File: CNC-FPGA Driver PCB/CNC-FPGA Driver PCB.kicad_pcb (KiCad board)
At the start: 2 copper layers, 73.5 x 87 mm, 16 parts

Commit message: updated pcb traces
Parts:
- -  12V  +: renamed from 12V Power Supply
- A4988 X Axis Driver: value A4988 Stepper Driver -> A4988 N Axis Driver
- C1: renamed from 100[µF]; value C1 -> +100[µF]-
- renumbered 100[µF] to +100[µF]-
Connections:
- A4988 X Axis Driver pad 10: /SLP -> +3.3V
- A4988 Y Axis Driver pad 10: /SLP -> +3.3V
- A4988 Z Axis Driver pad 10: /SLP -> +3.3V
- JA pad 1: /MS1 -> /MS1 
- JA pad 10: +3.3V -> /LS+
- LimitSwitchX pad 1: +3.3V -> /LS+
- LimitSwitchY pad 1: +3.3V -> /LS+
- LimitSwitchZ pad 1: +3.3V -> /LS+
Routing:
- net /LS+: track 0.00 -> 4.84 mm
- net +3.3V: track 14.5 -> 9.68 mm
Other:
- board size 73.5 x 87 mm -> 70 x 85 mm

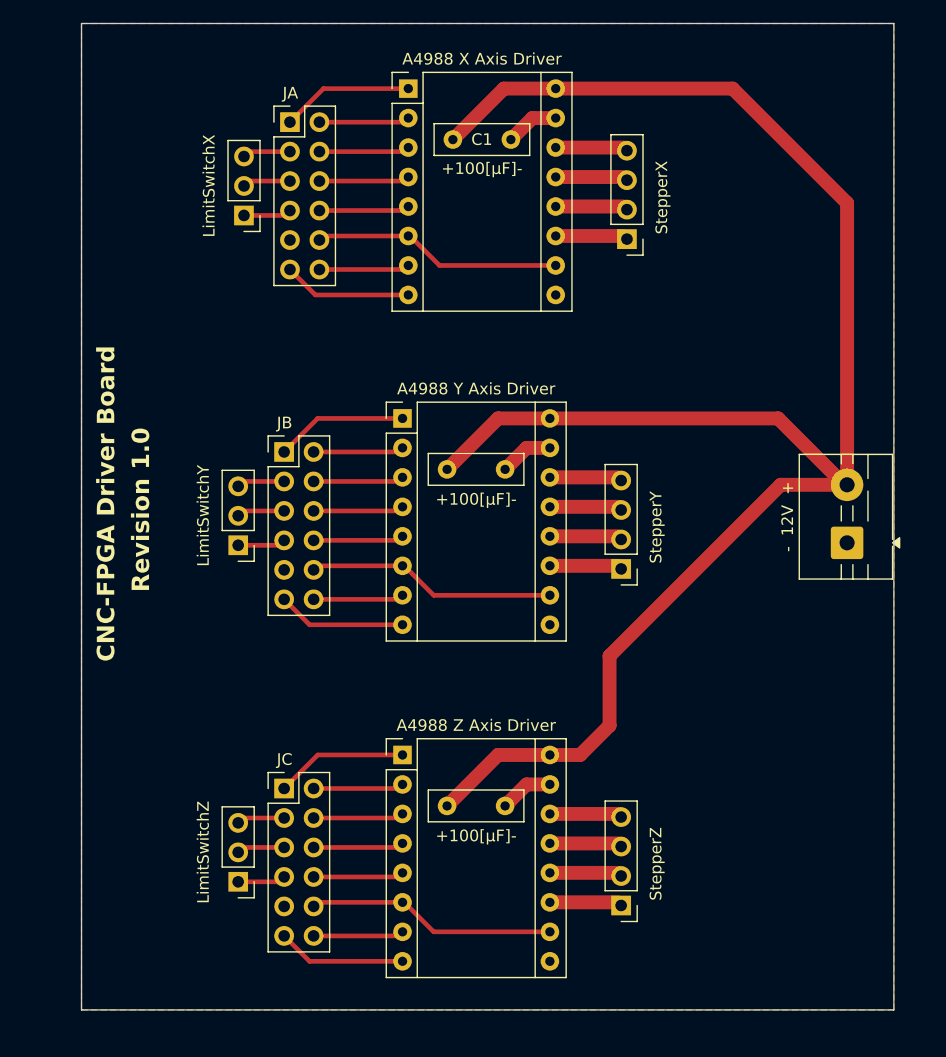
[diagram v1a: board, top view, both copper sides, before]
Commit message: added M2 mounting holes to pcb
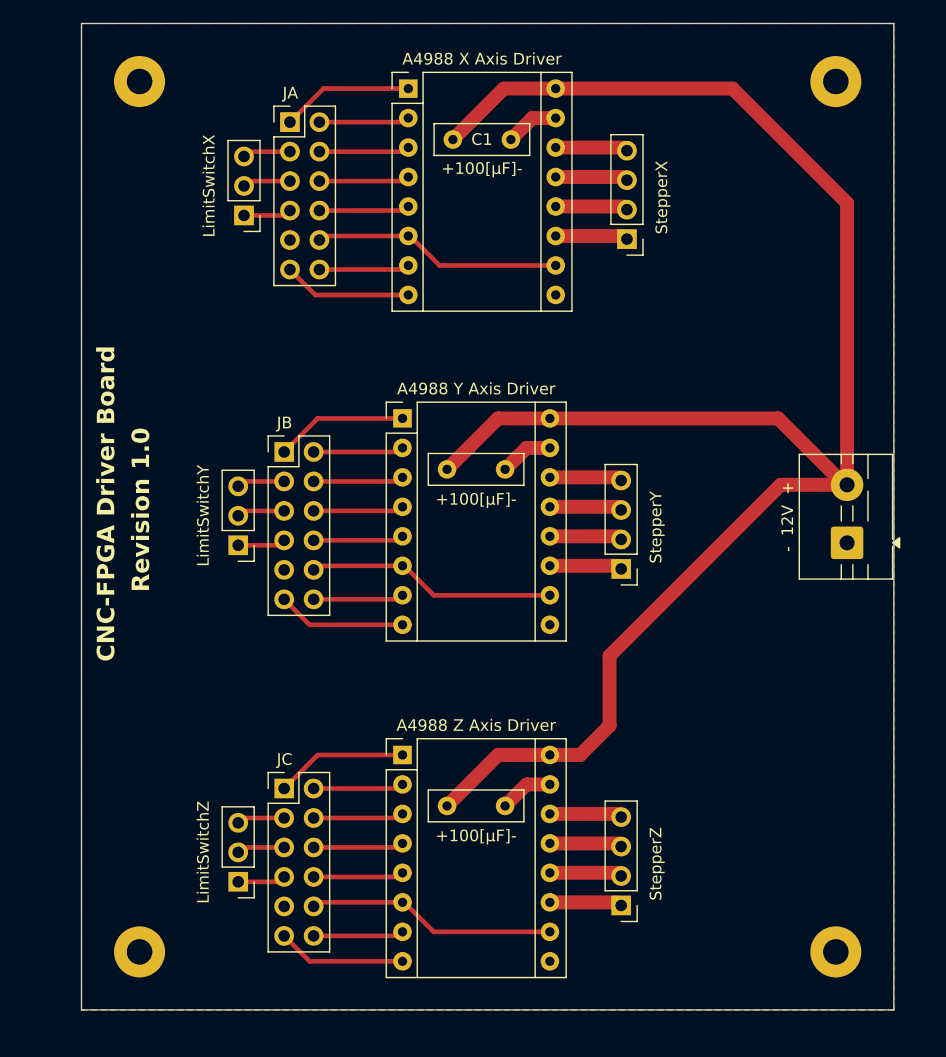
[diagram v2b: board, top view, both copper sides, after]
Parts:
- added REF**: MountingHole_2.2mm_M2_Pad, MountingHole:MountingHole_2.2mm_M2_Pad, F.Cu at (202.5, 80.0)
- added REF**: MountingHole_2.2mm_M2_Pad, MountingHole:MountingHole_2.2mm_M2_Pad, F.Cu at (262.5, 155.0)
- added REF**: MountingHole_2.2mm_M2_Pad, MountingHole:MountingHole_2.2mm_M2_Pad, F.Cu at (262.5, 80.0)
- added REF**: MountingHole_2.2mm_M2_Pad, MountingHole:MountingHole_2.2mm_M2_Pad, F.Cu at (202.5, 155.0)

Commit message: some pcb improvements, text & cut corners
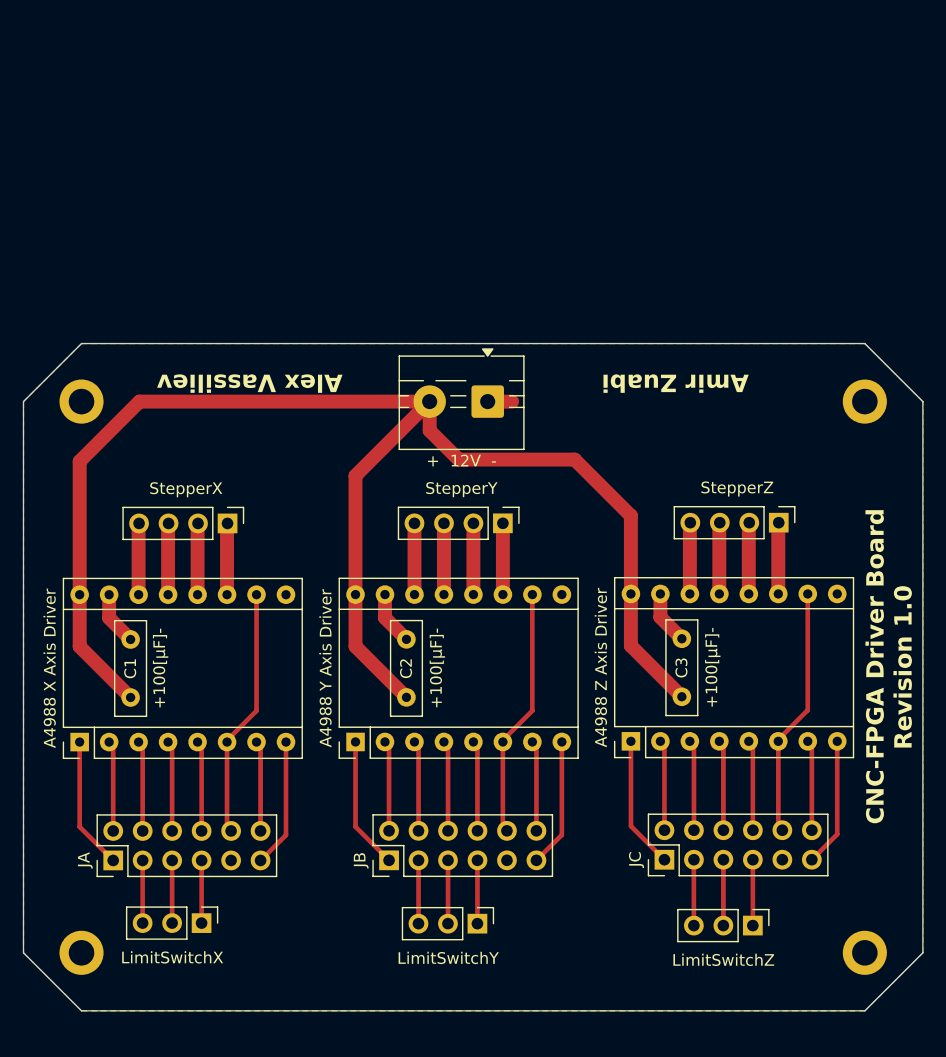
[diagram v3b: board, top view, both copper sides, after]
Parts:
- removed the REF** at (202.5, 80.0)
- removed the REF** at (262.5, 155.0)
- removed the REF** at (262.5, 80.0)
- removed the REF** at (202.5, 155.0)
- added REF**: MountingHole_2.2mm_M2_DIN965_Pad, MountingHole:MountingHole_2.2mm_M2_DIN965_Pad, F.Cu at (265.0, 107.6)
- added REF**: MountingHole_2.2mm_M2_DIN965_Pad, MountingHole:MountingHole_2.2mm_M2_DIN965_Pad, F.Cu at (197.5, 107.6)
- added REF**: MountingHole_2.2mm_M2_DIN965_Pad, MountingHole:MountingHole_2.2mm_M2_DIN965_Pad, F.Cu at (197.5, 155.1)
- added REF**: MountingHole_2.2mm_M2_DIN965_Pad, MountingHole:MountingHole_2.2mm_M2_DIN965_Pad, F.Cu at (265.0, 155.1)
- +  12V  - : renamed from -  12V  +
- moved JA 65.4 mm to (200.2, 147.1), turned to 90 degrees
- moved A4988 X Axis Driver 63.0 mm to (197.3, 136.9), turned to 90 degrees
- moved LimitSwitchX 61.1 mm to (207.8, 152.5), turned to -90 degrees
- moved C1 55.5 mm to (201.7, 133.1), turned to 90 degrees
- moved LimitSwitchZ 44.5 mm to (255.3, 152.7), turned to -90 degrees
- moved StepperX 42.2 mm to (210.1, 118.1), turned to -90 degrees
- moved LimitSwitchY 38.6 mm to (231.6, 152.6), turned to -90 degrees
- moved JB 36.3 mm to (224.0, 147.1), turned to 90 degrees
- moved StepperZ 35.7 mm to (257.6, 118.0), turned to -90 degrees
- moved JC 33.3 mm to (247.7, 147.1), turned to 90 degrees
- moved +  12V  -  33.3 mm to (232.5, 107.6), turned to 180 degrees
- moved A4988 Y Axis Driver 28.2 mm to (221.1, 136.9), turned to 90 degrees
- moved +100[µF]- 22.3 mm to (249.2, 133.0), turned to 90 degrees
- moved +100[µF]- 20.0 mm to (225.5, 133.1), turned to 90 degrees
- moved A4988 Z Axis Driver 19.7 mm to (244.8, 136.9), turned to 90 degrees
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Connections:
- JB pad 10: +3.3V -> /LS+
- JC pad 10: +3.3V -> /LS+
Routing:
- net Net-(A1-VMOT): track 152.6 -> 124.9 mm
- net /LS+: track 4.84 -> 18.9 mm
- net +3.3V: track 9.68 -> 0.00 mm
- net /LSS: track 12.4 -> 16.5 mm
- net /LS-: track 12.6 -> 16.7 mm
- net GND: track 13.9 -> 16.0 mm
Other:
- board size 70 x 85 mm -> 77.5 x 57.5 mm
- board text added: "Alex Vassiliev"
- board text added: "Amir Zuabi"

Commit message: pcb updated to fit 2 motors on Z axis
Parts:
- added StepperZ_2: DuPont 1x4, Connector_PinHeader_2.54mm:PinHeader_1x04_P2.54mm_Vertical, F.Cu at (257.6, 112.0)
- renumbered StepperZ to StepperZ_1

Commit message: updated the PCB revision
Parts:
- A4988 Y Axis Driver: renamed from A4988 Z Axis Driver
- A4988 Z Axis Driver: renamed from A4988 Y Axis Driver
- renumbered LimitSwitchZ to LimitSwitchY, LimitSwitchY to LimitSwitchZ, StepperZ_1 to StepperY_1, StepperZ_2 to StepperY_2, StepperY to StepperZ
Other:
- board text added: "Revision 1.1"
- board text removed: "Revision 1.0"
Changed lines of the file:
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@@
 			(drillshape 0)
 			(scaleselection 1)
-			(outputdirectory "./")
+			(outputdirectory "Gerber/")
 		)
 	)
@@
 		(descr "Through hole straight pin header, 1x03, 2.54mm pitch, single row")
 		(tags "Through hole pin header THT 1x03 2.54mm single row")
-		(property "Reference" "LimitSwitchZ"
+		(property "Reference" "LimitSwitchY"
 			(at 3 2.54 0)
 			(layer "F.SilkS")
@@
 		(descr "Pololu Breakout 16-pin 15.2x20.3mm 0.6x0.8\\")
 		(tags "Pololu Breakout")
-		(property "Reference" "A4988 Z Axis Driver"
+		(property "Reference" "A4988 Y Axis Driver"
 			(at 6.35 -2.54 90)
 			(layer "F.SilkS")
@@
 		(descr "Through hole straight pin header, 1x04, 2.54mm pitch, single row")
 		(tags "Through hole pin header THT 1x04 2.54mm single row")
-		(property "Reference" "StepperZ_2"
+		(property "Reference" "StepperY_2"
 			(at -3 3.58 0)
 			(layer "F.SilkS")
@@
 		(descr "Through hole straight pin header, 1x04, 2.54mm pitch, single row")
 		(tags "Through hole pin header THT 1x04 2.54mm single row")
-		(property "Reference" "StepperY"
+		(property "Reference" "StepperZ"
 			(at -3 3.58 0)
 			(layer "F.SilkS")
@@
 		(descr "Pololu Breakout 16-pin 15.2x20.3mm 0.6x0.8\\")
 		(tags "Pololu Breakout")
-		(property "Reference" "A4988 Y Axis Driver"
+		(property "Reference" "A4988 Z Axis Driver"
 			(at 6.35 -2.54 90)
 			(layer "F.SilkS")
@@
 		(descr "Through hole straight pin header, 1x03, 2.54mm pitch, single row")
 		(tags "Through hole pin header THT 1x03 2.54mm single row")
-		(property "Reference" "LimitSwitchY"
+		(property "Reference" "LimitSwitchZ"
 			(at 3 2.54 0)
 			(layer "F.SilkS")
@@
 		(descr "Through hole straight pin header, 1x04, 2.54mm pitch, single row")
 		(tags "Through hole pin header THT 1x04 2.54mm single row")
-		(property "Reference" "StepperZ_1"
+		(property "Reference" "StepperY_1"
 			(at -3 3.58 0)
 			(layer "F.SilkS")
@@
 		)
 	)
-	(gr_text "Revision 1.0"
+	(gr_text "Revision 1.1"
 		(at 269.209217 137.579545 90)
 		(layer "F.SilkS")
